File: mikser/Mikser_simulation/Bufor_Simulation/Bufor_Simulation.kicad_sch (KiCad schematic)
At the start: 5 parts, among them U2 ${SIM.PARAMS}

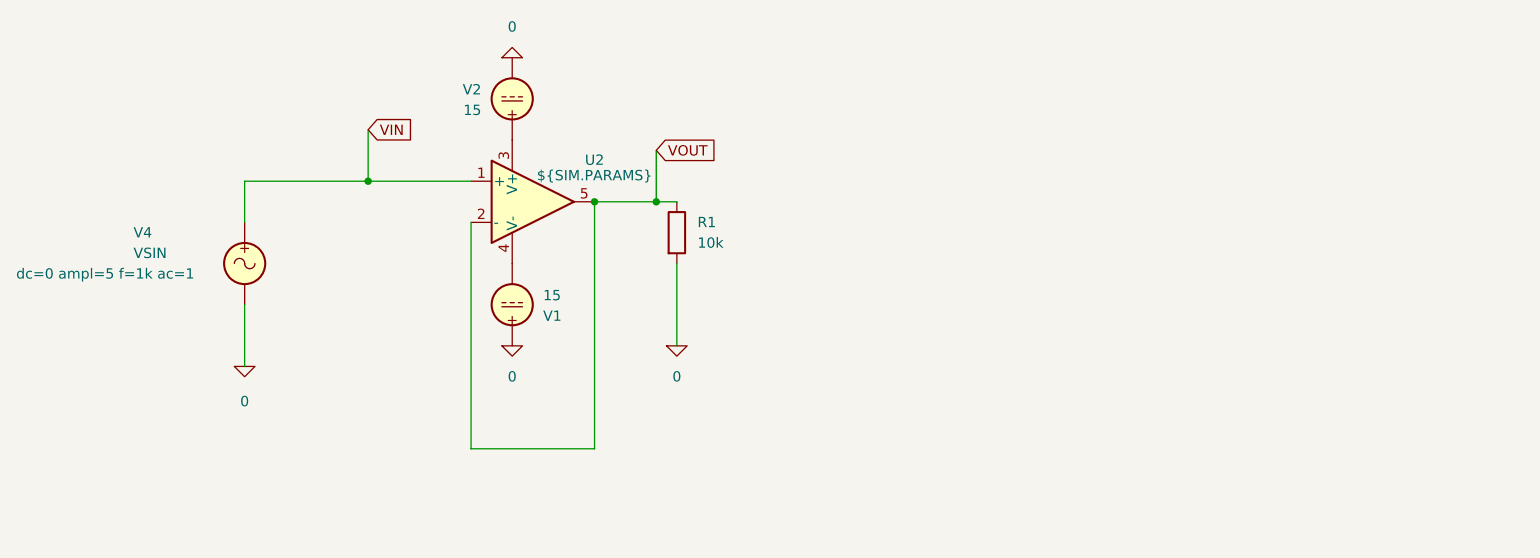
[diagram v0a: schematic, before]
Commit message: added coupling c and r to the simulation
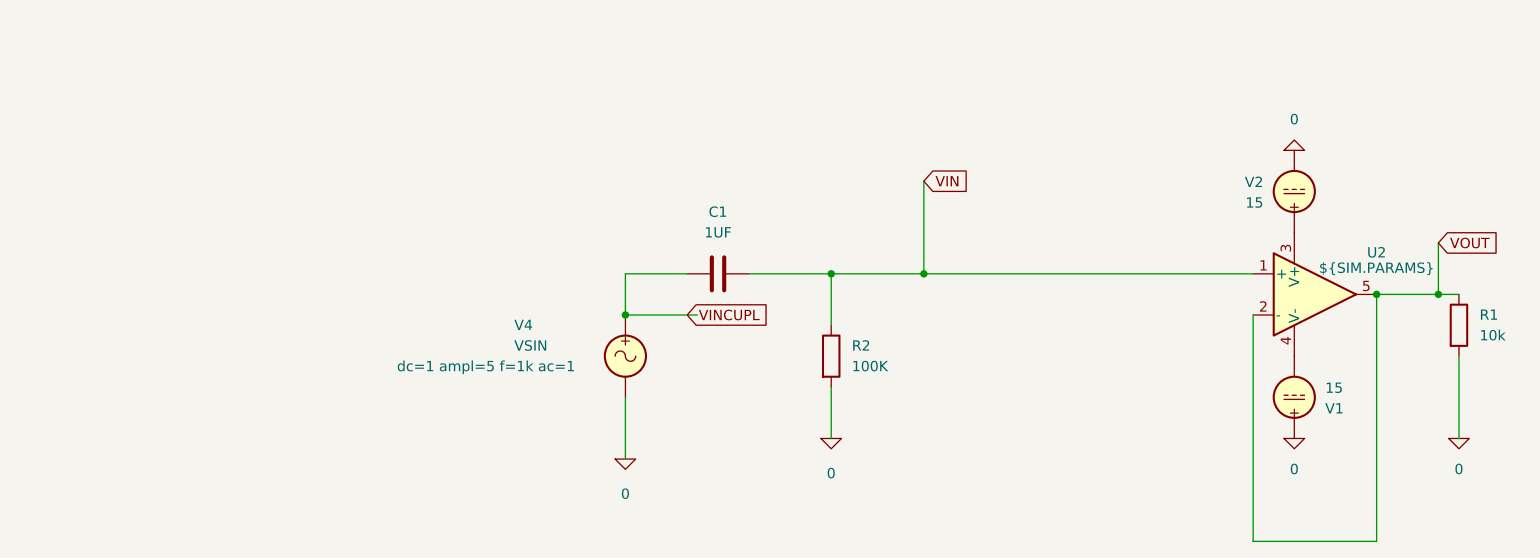
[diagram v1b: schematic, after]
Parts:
- added C1: 1UF, symbol Device:C
- added R2: 100K, symbol Device:R
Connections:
- net 0: now also R2.2
- net VIN: now also C1.2, R2.1; no longer V4.1
- new net VINCUPL: C1.1, V4.1
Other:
- moved on the sheet: R1, U2, V1, V2, V4

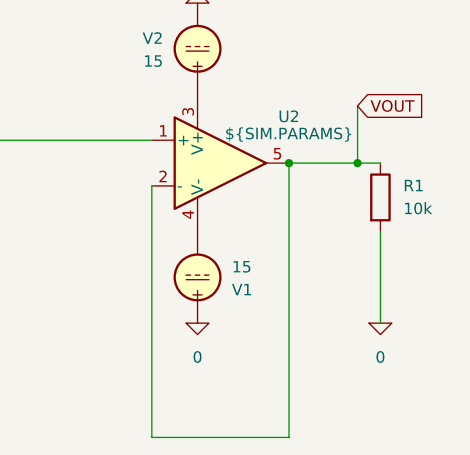
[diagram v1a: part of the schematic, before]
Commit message: added amplification sumulation
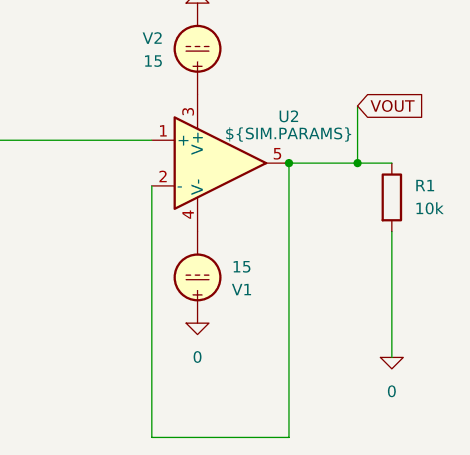
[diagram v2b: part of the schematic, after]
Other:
- moved on the sheet: R1
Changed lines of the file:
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@@
 	(wire
 		(pts
-			(xy 227.33 100.33) (xy 227.33 110.49)
+			(xy 228.6 100.33) (xy 228.6 114.3)
 		)
 		(stroke
@@
 	(wire
 		(pts
-			(xy 224.79 92.71) (xy 227.33 92.71)
+			(xy 224.79 92.71) (xy 228.6 92.71)
 		)
 		(stroke
@@
 	(symbol
 		(lib_id "Simulation_SPICE:0")
-		(at 227.33 110.49 0)
+		(at 228.6 114.3 0)
 		(unit 1)
 		(exclude_from_sim no)
@@
 		(dnp no)
 		(property "Reference" "#GND06"
-			(at 227.33 115.57 0)
+			(at 228.6 119.38 0)
 			(effects
 				(font
@@
 		)
 		(property "Value" "0"
-			(at 227.33 114.3 0)
+			(at 228.6 118.11 0)
 			(effects
 				(font
@@
 		)
 		(property "Footprint" ""
-			(at 227.33 110.49 0)
+			(at 228.6 114.3 0)
 			(effects
 				(font
@@
 		)
 		(property "Datasheet" "https://ngspice.sourceforge.io/docs/ngspice-html-manual/manual.xhtml#subsec_Circuit_elements__device"
-			(at 227.33 120.65 0)
+			(at 228.6 124.46 0)
 			(effects
 				(font
@@
 		)
 		(property "Description" "0V reference potential for simulation"
-			(at 227.33 118.11 0)
+			(at 228.6 121.92 0)
 			(effects
 				(font
@@
 	(symbol
 		(lib_id "Device:R")
-		(at 227.33 96.52 0)
+		(at 228.6 96.52 0)
 		(unit 1)
 		(exclude_from_sim no)
@@
 		(fields_autoplaced yes)
 		(property "Reference" "R1"
-			(at 229.87 95.2499 0)
+			(at 231.14 95.2499 0)
 			(effects
 				(font
@@
 		)
 		(property "Value" "10k"
-			(at 229.87 97.7899 0)
+			(at 231.14 97.7899 0)
 			(effects
 				(font
@@
 		)
 		(property "Footprint" ""
-			(at 225.552 96.52 90)
+			(at 226.822 96.52 90)
 			(effects
 				(font
@@
 		)
 		(property "Datasheet" "~"
-			(at 227.33 96.52 0)
+			(at 228.6 96.52 0)
 			(effects
 				(font
@@
 		)
 		(property "Description" "Resistor"
-			(at 227.33 96.52 0)
-			(effects
-				(font
+			(at 228.6 96.52 0)
+			(effects
+				(font
